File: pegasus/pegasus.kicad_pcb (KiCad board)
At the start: 2 copper layers, 52.5 x 109.2 mm, 10 parts, among them IC1 Adafruit_MPL3115A2, IC2 Adafruit-BNO055-PCB, IC3 L70B-M39, IC4 RFD900, J1 Conn_01x02_Female, J2 Conn_01x02_Female, J3 Conn_01x02_Female, J4 Conn_Coaxial, J5 Conn_Coaxial, U1 Teensy4.1

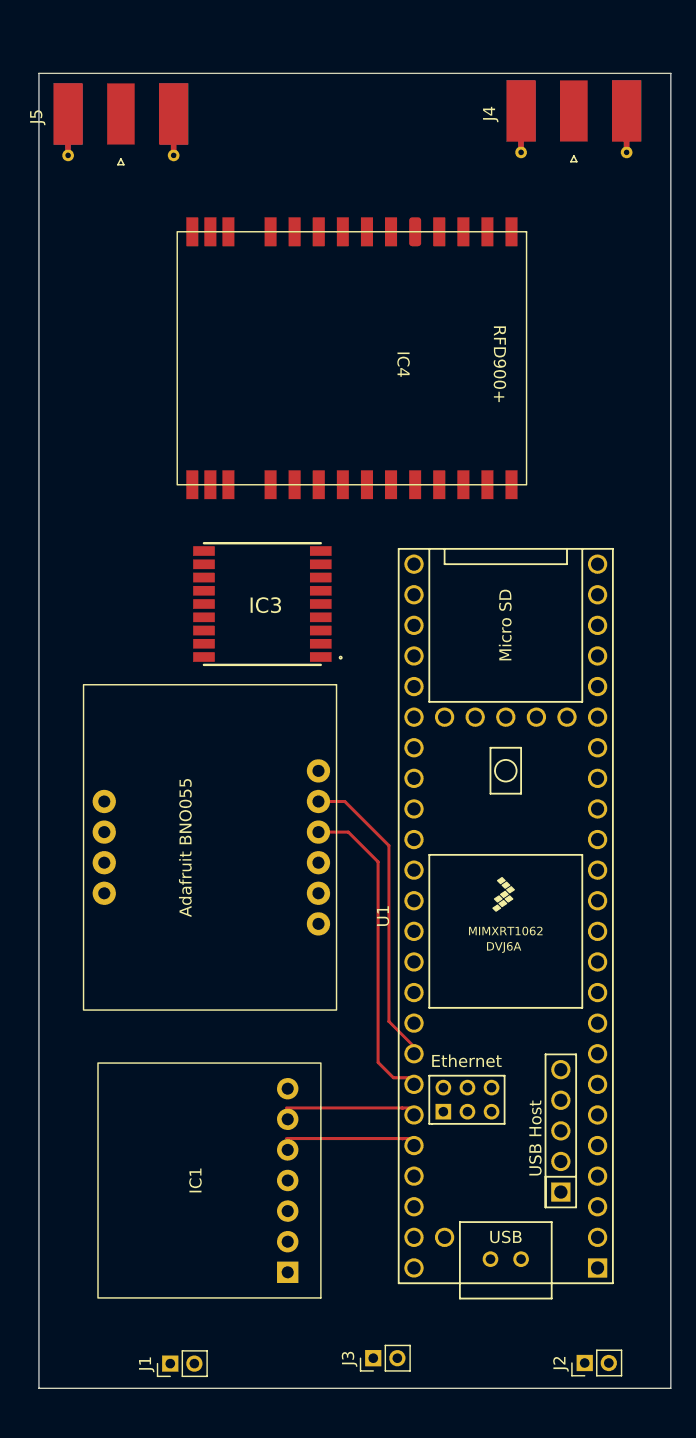
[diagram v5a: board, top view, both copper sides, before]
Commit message: added voltage regulator to schematic and pcb
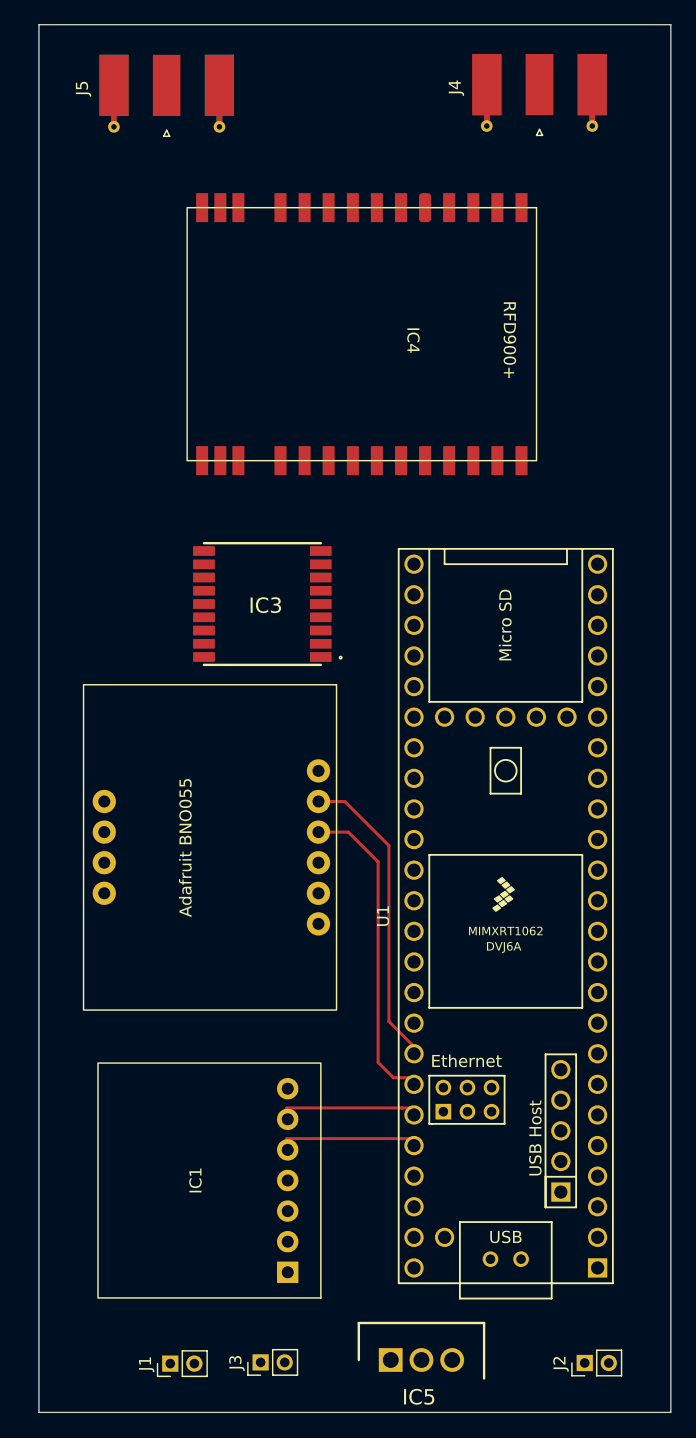
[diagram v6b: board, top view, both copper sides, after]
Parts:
- added IC5: L7805ACV, Voltage Regulator:TO255P460X1020X2008-3P, F.Cu at (106.4, 164.4)
- moved J3 9.36 mm to (95.6, 164.6)
- moved J5 4.48 mm to (87.8, 60.3)
- moved J4 3.59 mm to (118.8, 60.2)
- moved IC4 2.16 mm to (107.2, 74.8)
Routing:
- net unconnected-(U1-Pad44): track 10.7 -> 0.00 mm
- net unconnected-(U1-Pad43): track 10.7 -> 0.00 mm
- net unconnected-(IC1-Pad5): track 0.00 -> 10.7 mm
- net Net-(IC1-Pad6): track 0.00 -> 10.7 mm
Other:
- board size 52.5 x 109.2 mm -> 52.5 x 115.2 mm
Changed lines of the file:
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@@
   (net 105 "unconnected-(U1-Pad66)")
   (net 106 "unconnected-(U1-Pad67)")
+  (net 107 "/+7.4V")
   (footprint "Connector_Coaxial:SMA_Molex_73251-1153_EdgeMount_Horizontal" (layer "F.Cu")
-    (at 121.6 62.44 -90)
+    (at 118.75 60.25 -90)
     (descr "Molex SMA RF Connectors, Edge Mount, (http://www.molex.com/pdm_docs/sd/732511150_sd.pdf)")
     (tags "sma edge")
@@
       (net 39 "Net-(IC4-Pad15)") (pinfunction "Ext") (pintype "passive"))
     (model "${KICAD6_3DMODEL_DIR}/Connector_Coaxial.3dshapes/SMA_Molex_73251-1153_EdgeMount_Horizontal.wrl"
+      (offset (xyz 0 0 0))
+      (scale (xyz 1 1 1))
+      (rotate (xyz 0 0 0))
+    )
+  )
+  (footprint "Voltage Regulator:TO255P460X1020X2008-3P" (layer "F.Cu")
+    (at 106.4 164.4)
+    (descr "3-Pin TO-220")
+    (tags "Integrated Circuit")
+    (property "Allied_Number" "70013701")
+    (property "Description" "Linear voltage regulator,L7805ACV 5V 1A STMicroelectronics L7805ACV, Single Linear Voltage Regulator, 1A 5 V, 2%, 3-Pin TO-220")
+    (property "Height" "4.6")
+    (property "Manufacturer_Name" "STMicroelectronics")
+    (property "Manufacturer_Part_Number" "L7805ACV")
+    (property "RS Part Number" "2988508P")
+    (property "RS Price/Stock" "http://uk.rs-online.com/web/p/products/2988508P")
+    (property "Sheetfile" "pegasus.kicad_sch")
+    (property "Sheetname" "")
+    (attr through_hole)
+    (fp_text reference "IC5" (at 2.35 3.1) (layer "F.SilkS")
+      (effects (font (size 1.27 1.27) (thickness 0.254)))
+    )
+    (fp_text value "L7805ACV" (at 0 0) (layer "F.SilkS") hide
+      (effects (font (size 1.27 1.27) (thickness 0.254)))
+    )
+    (fp_text user "${REFERENCE}" (at 2.35 3.1) (layer "F.Fab")
+      (effects (font (size 1.27 1.27) (thickness 0.254)))
+    )
+    (fp_line (start 7.75 1.53) (end 7.75 -3.07) (layer "F.SilkS") (width 0.2))
+    (fp_line (start 7.75 -3.07) (end -2.65 -3.07) (layer "F.SilkS") (width 0.2))
+    (fp_line (start -2.65 -3.07) (end -2.65 0) (layer "F.SilkS") (width 0.2))
+    (fp_line (start -2.9 1.78) (end -2.9 -3.32) (layer "F.CrtYd") (width 0.05))
+    (fp_line (start 8 -3.32) (end 8 1.78) (layer "F.CrtYd") (width 0.05))
+    (fp_line (start 8 1.78) (end -2.9 1.78) (layer "F.CrtYd") (width 0.05))
+    (fp_line (start -2.9 -3.32) (end 8 -3.32) (layer "F.CrtYd") (width 0.05))
+    (fp_line (start -2.65 -1.795) (end -1.375 -3.07) (layer "F.Fab") (width 0.1))
+    (fp_line (start -2.65 1.53) (end -2.65 -3.07) (layer "F.Fab") (width 0.1))
+    (fp_line (start 7.75 1.53) (end -2.65 1.53) (layer "F.Fab") (width 0.1))
+    (fp_line (start -2.65 -3.07) (end 7.75 -3.07) (layer "F.Fab") (width 0.1))
+    (fp_line (start 7.75 -3.07) (end 7.75 1.53) (layer "F.Fab") (width 0.1))
+    (pad "1" thru_hole rect (at 0 0) (size 1.98 1.98) (drill 1.32) (layers *.Cu *.Mask)
+      (net 107 "/+7.4V") (pinfunction "INPUT") (pintype "passive"))
+    (pad "2" thru_hole circle (at 2.55 0) (size 1.98 1.98) (drill 1.32) (layers *.Cu *.Mask)
+      (net 2 "GND") (pinfunction "GND") (pintype "passive"))
+    (pad "3" thru_hole circle (at 5.1 0) (size 1.98 1.98) (drill 1.32) (layers *.Cu *.Mask)
+      (net 42 "/+5V") (pinfunction "OUTPUT") (pintype "passive"))
+    (model "C:\\Users\\usern\\Downloads\\schematic-symbol-and-pcb-footprint\\SamacSys_Parts.3dshapes\\L7805ACV.stp"
       (offset (xyz 0 0 0))
       (scale (xyz 1 1 1))
@@
   )
   (footprint "Connector_Coaxial:SMA_Molex_73251-1153_EdgeMount_Horizontal" (layer "F.Cu")
-    (at 84 62.69 -90)
+    (at 87.8 60.32 -90)
     (descr "Molex SMA RF Connectors, Edge Mount, (http://www.molex.com/pdm_docs/sd/732511150_sd.pdf)")
     (tags "sma edge")
@@
   )
   (footprint "RFD900:1x28" (layer "F.Cu")
-    (at 106.425 76.75 -90)
+    (at 107.25 74.75 -90)
     (property "Sheetfile" "pegasus.kicad_sch")
     (property "Sheetname" "")
@@
   )
   (footprint "Connector_PinHeader_2.00mm:PinHeader_1x02_P2.00mm_Vertical" (layer "F.Cu")
-    (at 104.95 164.25 90)
+    (at 95.6 164.6 90)
     (descr "Through hole straight pin header, 1x02, 2.00mm pitch, single row")
     (tags "Through hole pin header THT 1x02 2.00mm single row")
@@
     )
   )
-  (gr_rect (start 129.65 166.75) (end 77.2 57.6) (layer "Edge.Cuts") (width 0.1) (fill none))
+  (gr_rect (start 129.65 168.75) (end 77.2 53.56) (layer "Edge.Cuts") (width 0.1) (fill none))
+  (segment (start 108.35 146.02) (end 108.38 146.05) (width 0.25) (layer "F.Cu") (net 5))
+  (segment (start 107.35 146.02) (end 107.38 146.05) (width 0.25) (layer "F.Cu") (net 5))
+  (segment (start 97.74 146.02) (end 108.35 146.02) (width 0.25) (layer "F.Cu") (net 5))
+  (segment (start 107.35 143.48) (end 107.38 143.51) (width 0.25) (layer "F.Cu") (net 6))
+  (segment (start 108.35 143.48) (end 108.38 143.51) (width 0.25) (layer "F.Cu") (net 6))
+  (segment (start 97.74 143.48) (end 108.35 143.48) (width 0.25) (layer "F.Cu") (net 6))
   (segment (start 105.35 139.7) (end 106.62 140.97) (width 0.25) (layer "F.Cu") (net 9))
   (segment (start 105.35 123.05) (end 105.35 139.7) (width 0.25) (layer "F.Cu") (net 9))
@@
   (segment (start 100.4 118.04) (end 102.59 118.04) (width 0.25) (layer "F.Cu") (net 10))
   (segment (start 106.25 136.3) (end 108.38 138.43) (width 0.25) (layer "F.Cu") (net 10))
-  (segment (start 107.35 143.48) (end 107.38 143.51) (width 0.25) (layer "F.Cu") (net 85))
-  (segment (start 108.35 143.48) (end 108.38 143.51) (width 0.25) (layer "F.Cu") (net 85))
-  (segment (start 97.74 143.48) (end 108.35 143.48) (width 0.25) (layer "F.Cu") (net 85))
-  (segment (start 108.35 146.02) (end 108.38 146.05) (width 0.25) (layer "F.Cu") (net 86))
-  (segment (start 107.35 146.02) (end 107.38 146.05) (width 0.25) (layer "F.Cu") (net 86))
-  (segment (start 97.74 146.02) (end 108.35 146.02) (width 0.25) (layer "F.Cu") (net 86))
 )

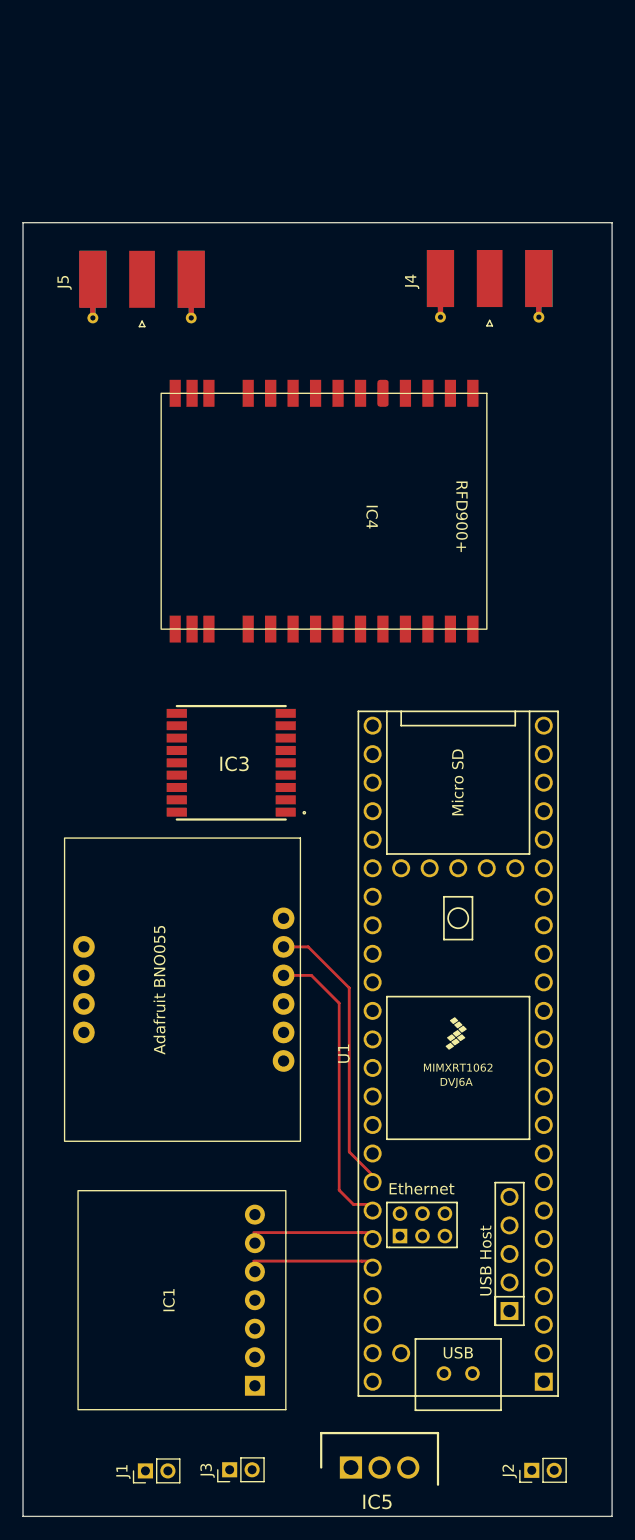
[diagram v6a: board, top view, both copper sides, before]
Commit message: removed one of connectors, fixed connector schematic wiring
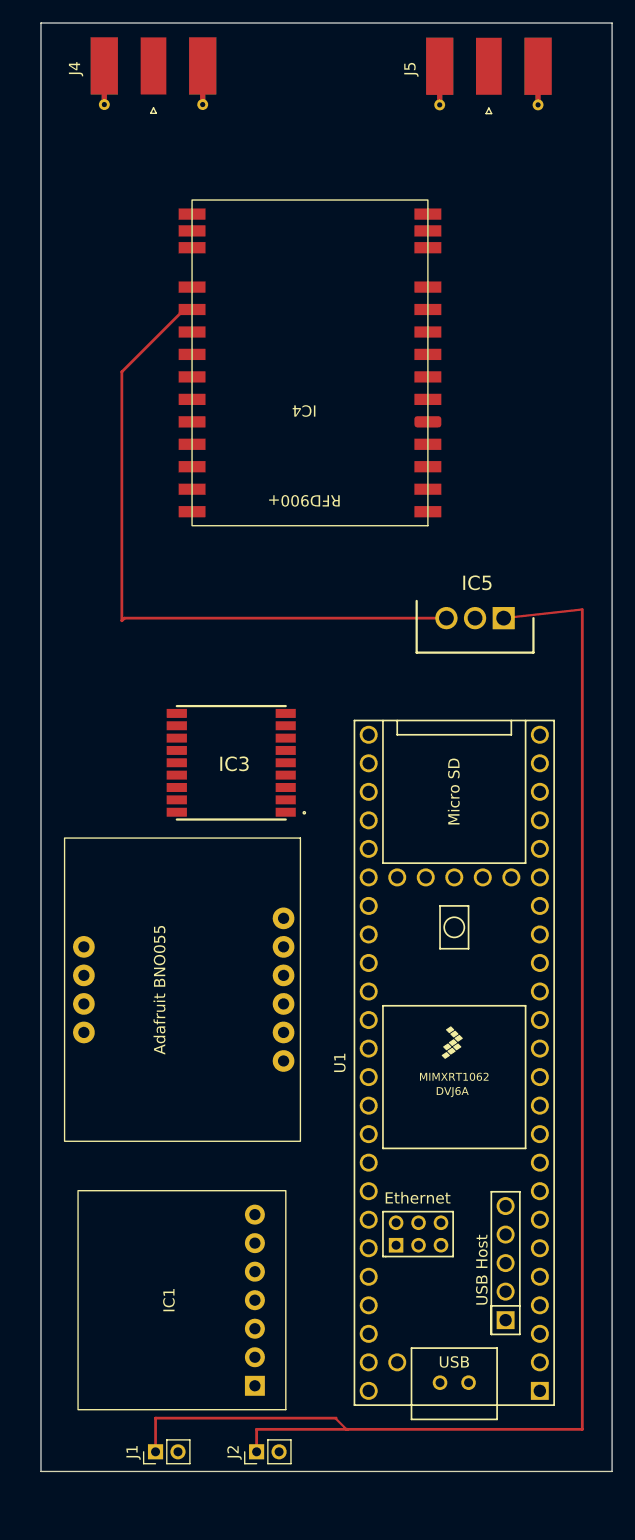
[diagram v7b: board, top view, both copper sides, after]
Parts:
- removed J3: Conn_01x02_Female, Connector_PinHeader_2.00mm:PinHeader_1x02_P2.00mm_Vertical
- moved IC5 76.8 mm to (120.0, 88.8), turned to 180 degrees
- moved J5 36.2 mm to (118.7, 41.4)
- moved J4 35.4 mm to (88.8, 41.3)
- moved J2 24.6 mm to (98.0, 163.0)
- moved IC4 5.46 mm to (107.2, 69.3), turned to 180 degrees
- moved J1 1.92 mm to (89.0, 163.0)
- moved U1 0.89 mm to (115.6, 128.4)
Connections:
- IC5 pad 1: /+7.4V -> 3.7V
- J1 pad 1: /+3.7V -> 3.7V
- J2 pad 1: /+3.7V -> 3.7V
- U1 pad 48: /+3.7V -> 3.7V
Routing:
- net 3.7V: track 0.00 -> 123.2 mm
- net /+5V: track 0.00 -> 59.7 mm
- net Net-(IC2-Pad4)_1: track 26.2 -> 0.00 mm
- net Net-(IC2-Pad5)_1: track 25.0 -> 0.00 mm
- net unconnected-(IC1-Pad5): track 10.7 -> 0.00 mm
- net Net-(IC1-Pad6): track 10.7 -> 0.00 mm
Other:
- board size 52.5 x 115.2 mm -> 50.8 x 129 mm

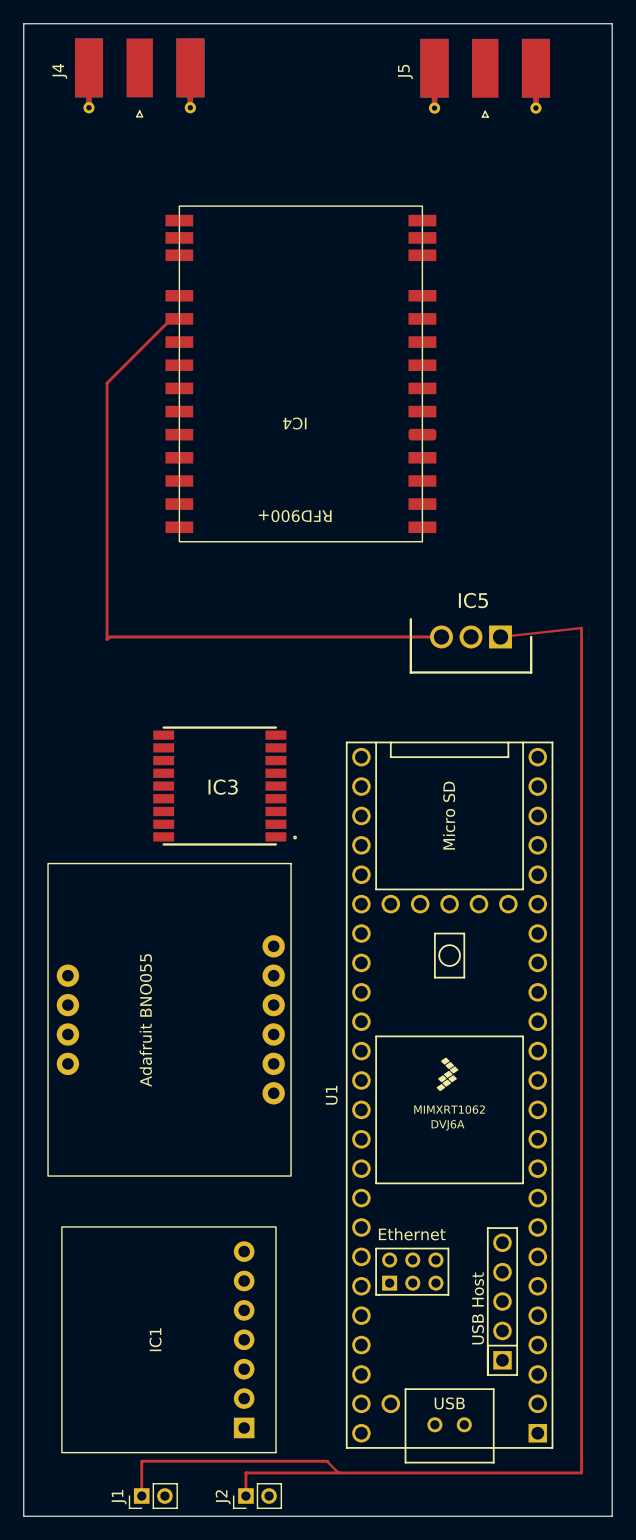
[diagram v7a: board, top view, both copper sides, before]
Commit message: created sma-connector schematic and footprint and implemented 3D step file
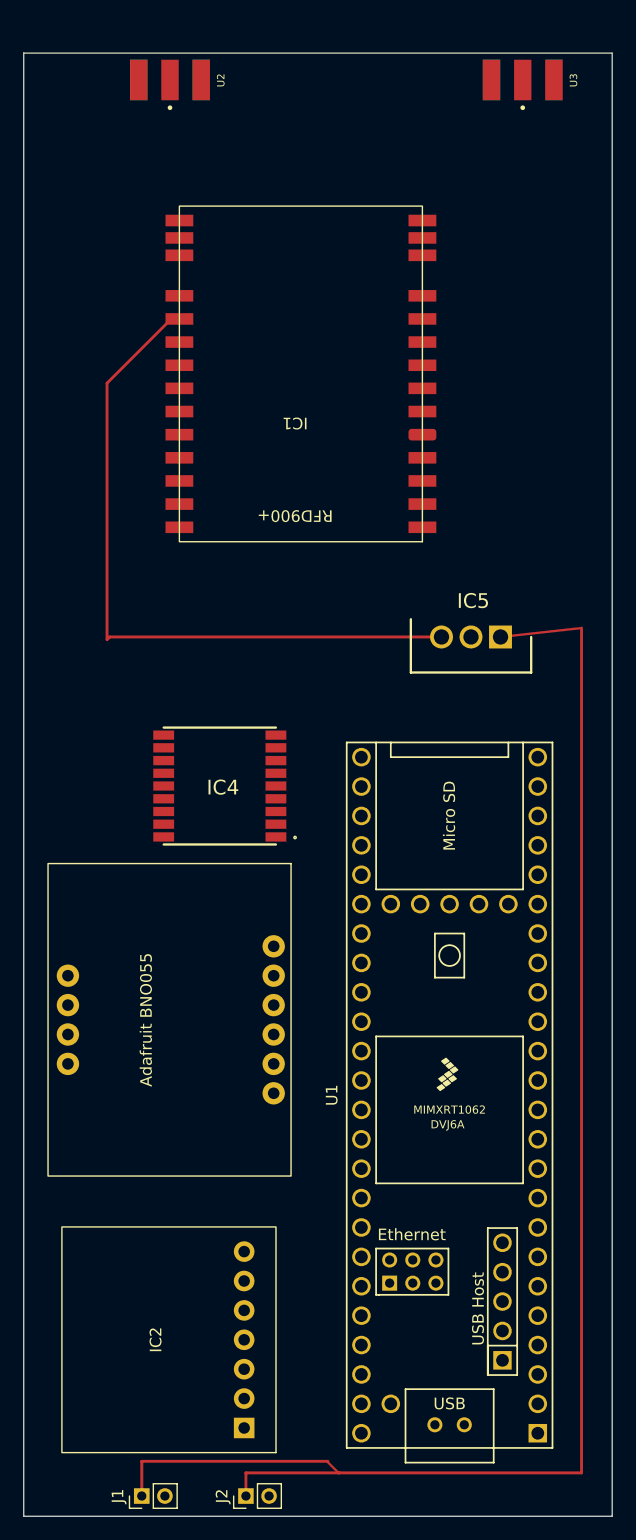
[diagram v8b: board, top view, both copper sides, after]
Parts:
- removed J4, J5: Conn_Coaxial, Connector_Coaxial:SMA_Molex_73251-1153_EdgeMount_Horizontal
- added U2: CON-SMA-EDGE-S, SMA-Connectors:RFSOLUTIONS_CON-SMA-EDGE-S, F.Cu at (91.4, 40.6)
- added U3: CON-SMA-EDGE-S, SMA-Connectors:RFSOLUTIONS_CON-SMA-EDGE-S, F.Cu at (121.9, 40.6)
- renumbered IC4 to IC1, IC1 to IC2, IC2 to IC3, IC3 to IC4
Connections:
- IC1 pad 12: Net-(IC4-Pad12) -> Net-(IC1-Pad12)
- IC1 pad 14: Net-(IC4-Pad12) -> Net-(IC1-Pad14)
- IC1 pad 15: Net-(IC4-Pad15) -> Net-(IC1-Pad15)
- IC1 pad 17: Net-(IC4-Pad15) -> Net-(IC1-Pad17)
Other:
- board size 50.8 x 129 mm -> 50.8 x 126.4 mm
